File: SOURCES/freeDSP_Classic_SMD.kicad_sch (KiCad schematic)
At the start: 51 parts, among them P1 CONN_01X06, P10 CONN_02X03, P11 CONN_02X03, P12 CONN_02X03, P13 CONN_02X03, P2 CONN_01X03, P3 CONN_02X05, P4 STDCONN, P5 STDCONN, P6 STDCONN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

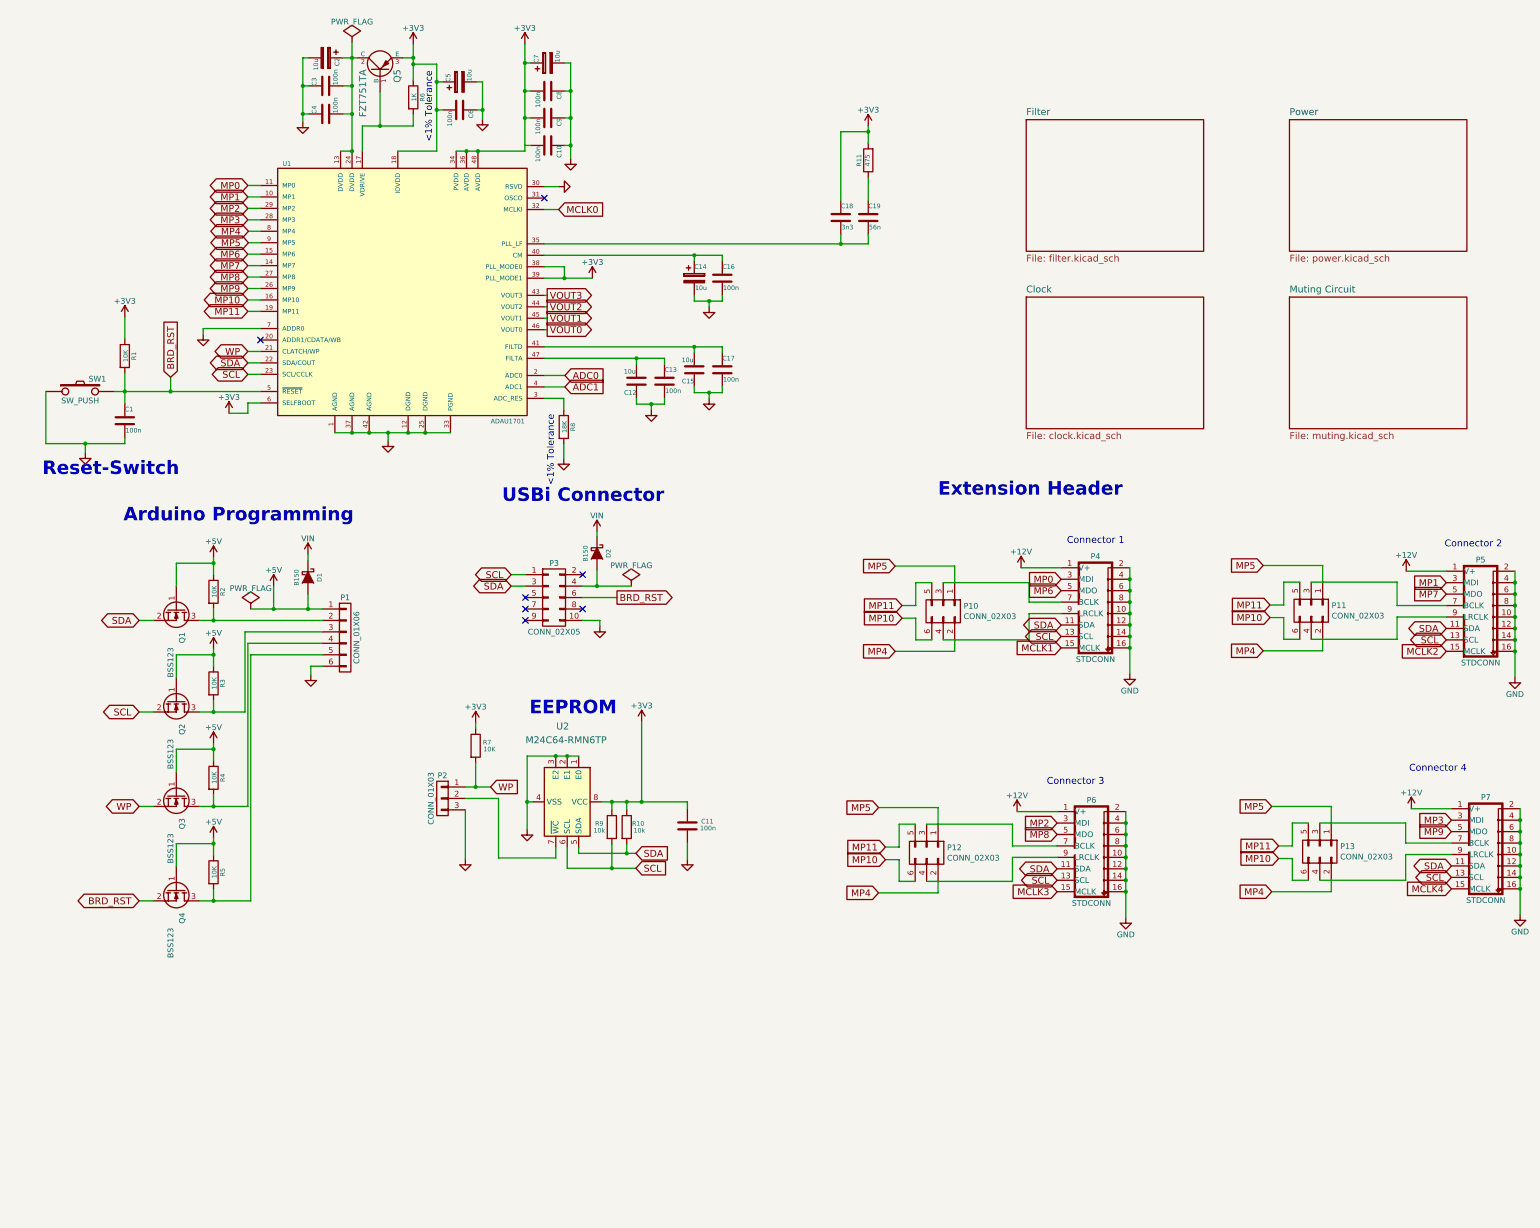
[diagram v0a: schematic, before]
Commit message: More updates
Updated some symbols and components, as well as redid some layout to accommodate those symbol changes
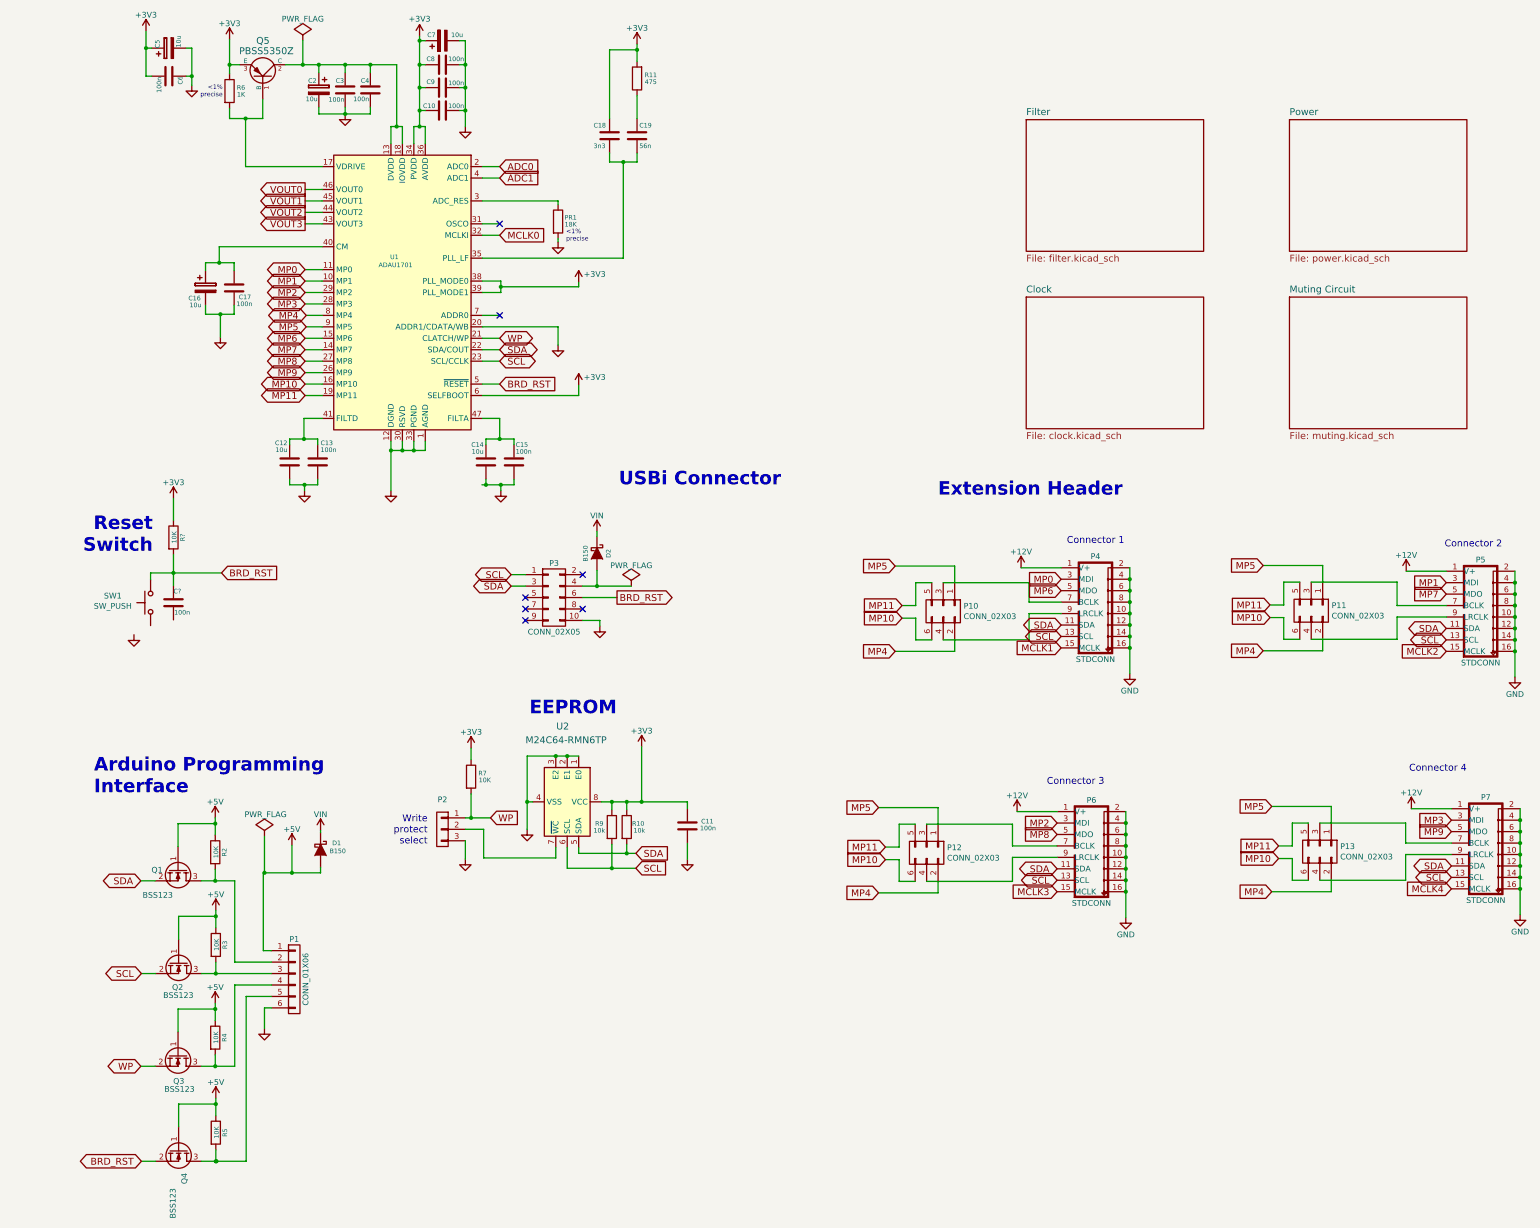
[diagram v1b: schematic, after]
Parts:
- removed C1, C13: 100n, fdsp_capacitor:C_1206_HandSoldering, symbol freeDSP_Classic_SMD-rescue:C
- removed C12: 10u, fdsp_capacitor:C_1206_HandSoldering, symbol freeDSP_Classic_SMD-rescue:C
- removed R1: 10K, fdsp_resistor:R_1206_HandSoldering, symbol freeDSP_Classic_SMD-rescue:R
- removed R8: 18K, fdsp_resistor:R_1206_HandSoldering, symbol freeDSP_Classic_SMD-rescue:R
- removed SW1: SW_PUSH, fdsp_housing_new:SW_PUSH_6mm, symbol freeDSP_Classic_SMD-rescue:SW_PUSH
- added C14: 10u, fdsp_capacitor:C_1206_HandSoldering, symbol freeDSP_Classic_SMD-rescue:C
- added C15, C?: 100n, fdsp_capacitor:C_1206_HandSoldering, symbol freeDSP_Classic_SMD-rescue:C
- added PR1: 18K, fdsp_resistor:R_1206_HandSoldering, symbol freeDSP_Classic_SMD-rescue:R
- added R?: 10K, fdsp_resistor:R_1206_HandSoldering, symbol freeDSP_Classic_SMD-rescue:R
- added SW1: SW_PUSH, Button_Switch_THT:SW_PUSH_6mm, symbol Switch:SW_Push
- Q5: value FZT751TA -> PBSS5350Z
- U1: footprint fdsp_housing_new:LQFP-48_7x7mm_Pitch0.5mm -> Package_QFP:LQFP-48_7x7mm_P0.5mm; symbol freeDSP_Classic_SMD-rescue:ADAU1701 -> DSP_AnalogDevices:ADAU1701
- renumbered C15 to C12, C17 to C13, C14 to C16, C16 to C17
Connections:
- net +3V3: now also C10.2, R?.1; no longer U1.18 (IOVDD)
- net BRD_RST: now also C?.1, R?.2, SW1.2
- net GND: now also C3.2, C4.2, U1.20 (ADDR1/CDATA/WB), C14.1, C15.2, PR1.2; no longer C3.1, C4.1, U1.7 (ADDR0)
- net at C2.1, Q5.2 (C), U1.13 (DVDD)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: now also C3.1, C4.1, U1.18 (IOVDD); no longer C3.2, C4.2
- net at U1.3 (ADC_RES): now also PR1.1
- net at U1.47 (FILTA): now also C14.2, C15.1
- net at Q4.3 (D), R5.2: no longer P1.5 (P5)
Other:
- note added: "<1% precise"
- note added: "Arduino Programming Interface"
- note added: "Reset Switch"
- note added: "Write protect select"
- note removed: "<1% Tolerance"
- note removed: "Arduino Programming"
- note removed: "Reset-Switch"
- moved on the sheet: C10, C12, C13, C16, C17, C18, C19, C2, C3, C4, C5, C6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
